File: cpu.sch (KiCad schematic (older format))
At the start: 12 parts, among them SW2 RESET_SW, U10 NE555, U2 MOS_8501, U9 74LS06

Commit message: Fix for KiCad 5.1.7
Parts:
- removed U10: NE555, Package_DIP:DIP-8_W7.62mm_Socket_LongPads, symbol Timer:NE555
- added U10: NE555P, Package_DIP:DIP-8_W7.62mm_LongPads, symbol Timer:NE555P
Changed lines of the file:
@@
 Sheet 2 11
 Title "LittleSixteen"
-Date "2020-01-03"
+Date "2020-12-20"
 Rev "1git"
 Comp "SukkoPera"
@@
 PHI0
 $Comp
-L Timer:NE555 U10
-U 1 1 5EC2982D
-P 7885 2420
-F 0 "U10" H 7625 2765 50  0000 C CNN
-F 1 "NE555" H 7660 2070 50  0000 C CNN
-F 2 "Package_DIP:DIP-8_W7.62mm_Socket_LongPads" H 7885 2420 50  0001 C CNN
-F 3 "http://www.ti.com/lit/ds/symlink/ne555.pdf" H 7885 2420 50  0001 C CNN
-	1    7885 2420
-	-1   0    0    -1
-$EndComp
-$Comp
 L 74xx:74LS06 U9
 U 1 1 5EC2AC8D
@@
 Text GLabel 6320 1435 2    50   Output ~ 0
 ~RESET
+$Comp
+L Timer:NE555P U10
+U 1 1 5FE24901
+P 7885 2420
+F 0 "U10" H 7610 2770 50  0000 C CNN
+F 1 "NE555P" H 7685 2065 50  0000 C CNN
+F 2 "Package_DIP:DIP-8_W7.62mm_LongPads" H 8535 2020 50  0001 C CNN
+F 3 "http://www.ti.com/lit/ds/symlink/ne555.pdf" H 8735 2020 50  0001 C CNN
+	1    7885 2420
+	-1   0    0    -1
+$EndComp
 Wire Bus Line
 	5035 4120 5035 4580

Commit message: Start working on PCB
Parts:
- C16, C17, C4: footprint (none) -> Capacitor_THT:CP_Radial_D6.3mm_P2.50mm
- R19, R20, R21: footprint (none) -> Resistor_THT:R_Axial_DIN0207_L6.3mm_D2.5mm_P5.08mm_Vertical
- RP1: footprint (none) -> Resistor_THT:R_Array_SIP6
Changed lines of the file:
@@
 F 0 "C4" H 911 7136 50  0000 R CNN
 F 1 "10u/25V" H 911 7045 50  0000 R CNN
-F 2 "" H 1025 7090 50  0001 C CNN
+F 2 "Capacitor_THT:CP_Radial_D6.3mm_P2.50mm" H 1025 7090 50  0001 C CNN
 F 3 "~" H 1025 7090 50  0001 C CNN
 	1    1025 7090
@@
 F 0 "R19" H 2355 2016 50  0000 R CNN
 F 1 "3.3k" H 2355 1925 50  0000 R CNN
-F 2 "" V 2355 1970 50  0001 C CNN
+F 2 "Resistor_THT:R_Axial_DIN0207_L6.3mm_D2.5mm_P5.08mm_Vertical" V 2355 1970 50  0001 C CNN
 F 3 "~" H 2425 1970 50  0001 C CNN
 	1    2425 1970
@@
 F 0 "C16" H 7200 2981 50  0000 L CNN
 F 1 "10u/25V" H 7200 2890 50  0000 L CNN
-F 2 "" H 7085 2935 50  0001 C CNN
+F 2 "Capacitor_THT:CP_Radial_D6.3mm_P2.50mm" H 7085 2935 50  0001 C CNN
 F 3 "~" H 7085 2935 50  0001 C CNN
 	1    7085 2935
@@
 F 0 "R20" H 7155 1971 50  0000 L CNN
 F 1 "47k" H 7155 1880 50  0000 L CNN
-F 2 "" V 7015 1925 50  0001 C CNN
+F 2 "Resistor_THT:R_Axial_DIN0207_L6.3mm_D2.5mm_P5.08mm_Vertical" V 7015 1925 50  0001 C CNN
 F 3 "~" H 7085 1925 50  0001 C CNN
 	1    7085 1925
@@
 F 0 "R21" H 9525 1971 50  0000 L CNN
 F 1 "100k" H 9525 1880 50  0000 L CNN
-F 2 "" V 9385 1925 50  0001 C CNN
+F 2 "Resistor_THT:R_Axial_DIN0207_L6.3mm_D2.5mm_P5.08mm_Vertical" V 9385 1925 50  0001 C CNN
 F 3 "~" H 9455 1925 50  0001 C CNN
 	1    9455 1925
@@
 F 0 "C17" H 8961 2731 50  0000 R CNN
 F 1 "1u/16V" H 8961 2640 50  0000 R CNN
-F 2 "" H 9075 2685 50  0001 C CNN
+F 2 "Capacitor_THT:CP_Radial_D6.3mm_P2.50mm" H 9075 2685 50  0001 C CNN
 F 3 "~" H 9075 2685 50  0001 C CNN
 	1    9075 2685
@@
 F 0 "RP1" H 4613 1966 50  0000 L CNN
 F 1 "1k" H 4613 1875 50  0000 L CNN
-F 2 "" V 4455 1920 50  0001 C CNN
+F 2 "Resistor_THT:R_Array_SIP6" V 4455 1920 50  0001 C CNN
 F 3 "~" H 4525 1920 50  0001 C CNN
 	1    4525 1920

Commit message: Add ceramics
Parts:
- C22: footprint (none) -> Capacitor_THT:C_Disc_D8.0mm_W2.5mm_P5.00mm
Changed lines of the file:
@@
 F 0 "C22" H 1635 7136 50  0000 L CNN
 F 1 "100n" H 1635 7045 50  0000 L CNN
-F 2 "" H 1558 6940 50  0001 C CNN
+F 2 "Capacitor_THT:C_Disc_D8.0mm_W2.5mm_P5.00mm" H 1558 6940 50  0001 C CNN
 F 3 "~" H 1520 7090 50  0001 C CNN
 	1    1520 7090

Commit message: Use 3d models from github.com/StormTrooper/Commodore-Plus4
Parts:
- SW2: footprint (none) -> CommodorePlus4:Switch-Pushbutton
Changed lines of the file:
@@
 F 0 "SW2" V 9409 2793 50  0000 L CNN
 F 1 "RESET_SW" V 9500 2793 50  0000 L CNN
-F 2 "" H 9455 2685 60  0001 C CNN
+F 2 "CommodorePlus4:Switch-Pushbutton" H 9455 2685 60  0001 C CNN
 F 3 "" H 9455 2685 60  0000 C CNN
 	1    9455 2685

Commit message: Working on PCB...
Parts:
- SW2: footprint CommodorePlus4:Switch-Pushbutton -> LittleSixteen:Switch-Pushbutton
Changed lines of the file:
@@
 F 0 "SW2" V 9409 2793 50  0000 L CNN
 F 1 "RESET_SW" V 9500 2793 50  0000 L CNN
-F 2 "CommodorePlus4:Switch-Pushbutton" H 9455 2685 60  0001 C CNN
+F 2 "LittleSixteen:Switch-Pushbutton" H 9455 2685 60  0001 C CNN
 F 3 "" H 9455 2685 60  0000 C CNN
 	1    9455 2685

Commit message: A whole looooooot of work
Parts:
- U10: footprint Package_DIP:DIP-8_W7.62mm_LongPads -> Package_DIP:DIP-8_W7.62mm_Socket_LongPads
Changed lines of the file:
@@
 F 0 "U10" H 7610 2770 50  0000 C CNN
 F 1 "NE555P" H 7685 2065 50  0000 C CNN
-F 2 "Package_DIP:DIP-8_W7.62mm_LongPads" H 8535 2020 50  0001 C CNN
+F 2 "Package_DIP:DIP-8_W7.62mm_Socket_LongPads" H 8535 2020 50  0001 C CNN
 F 3 "http://www.ti.com/lit/ds/symlink/ne555.pdf" H 8735 2020 50  0001 C CNN
 	1    7885 2420

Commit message: Add extra decoupling caps There are actually (unnamed) footprints for these on an actual board, I guess they were skipped for cost saving reasons, sigh...
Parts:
- added C29: 100n, Capacitor_THT:C_Disc_D8.0mm_W2.5mm_P5.00mm, symbol Device:C
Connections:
- net GND: now also C29.2
- net VCC: now also C29.1
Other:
- note added: "Additional\ndecoupling cap\nfor U10"
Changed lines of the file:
@@
 Sheet 2 11
 Title "LittleSixteen"
-Date "2020-12-20"
+Date "2021-07-20"
 Rev "1git"
 Comp "SukkoPera"
@@
 	-1   0    0    -1
 $EndComp
+Wire Wire Line
+	10455 2595 10455 2670
+Wire Wire Line
+	10455 2220 10455 2295
+$Comp
+L power:GND #PWR?
+U 1 1 611CBEE7
+P 10455 2670
+AR Path="/5E4A465A/611CBEE7" Ref="#PWR?"  Part="1"
+AR Path="/5EE7AAEB/611CBEE7" Ref="#PWR?"  Part="1"
+AR Path="/5E4A81E1/611CBEE7" Ref="#PWR0133"  Part="1"
+F 0 "#PWR0133" H 10455 2420 50  0001 C CNN
+F 1 "GND" H 10460 2497 50  0000 C CNN
+F 2 "" H 10455 2670 50  0001 C CNN
+F 3 "" H 10455 2670 50  0001 C CNN
+	1    10455 2670
+	1    0    0    -1
+$EndComp
+$Comp
+L power:VCC #PWR?
+U 1 1 611CBEED
+P 10455 2220
+AR Path="/5E4A465A/611CBEED" Ref="#PWR?"  Part="1"
+AR Path="/5EE7AAEB/611CBEED" Ref="#PWR?"  Part="1"
+AR Path="/5E4A81E1/611CBEED" Ref="#PWR0134"  Part="1"
+F 0 "#PWR0134" H 10455 2070 50  0001 C CNN
+F 1 "VCC" H 10472 2393 50  0000 C CNN
+F 2 "" H 10455 2220 50  0001 C CNN
+F 3 "" H 10455 2220 50  0001 C CNN
+	1    10455 2220
+	1    0    0    -1
+$EndComp
+$Comp
+L Device:C C?
+U 1 1 611CBEF3
+P 10455 2445
+AR Path="/5E4A465A/611CBEF3" Ref="C?"  Part="1"
+AR Path="/5EE7AAEB/611CBEF3" Ref="C?"  Part="1"
+AR Path="/5E4A81E1/611CBEF3" Ref="C29"  Part="1"
+F 0 "C29" H 10570 2491 50  0000 L CNN
+F 1 "100n" H 10570 2400 50  0000 L CNN
+F 2 "Capacitor_THT:C_Disc_D8.0mm_W2.5mm_P5.00mm" H 10493 2295 50  0001 C CNN
+F 3 "~" H 10455 2445 50  0001 C CNN
+	1    10455 2445
+	1    0    0    -1
+$EndComp
+Text Notes 10225 3190 0    50   ~ 0
+Additional\ndecoupling cap\nfor U10
 Wire Bus Line
 	5035 4120 5035 4580

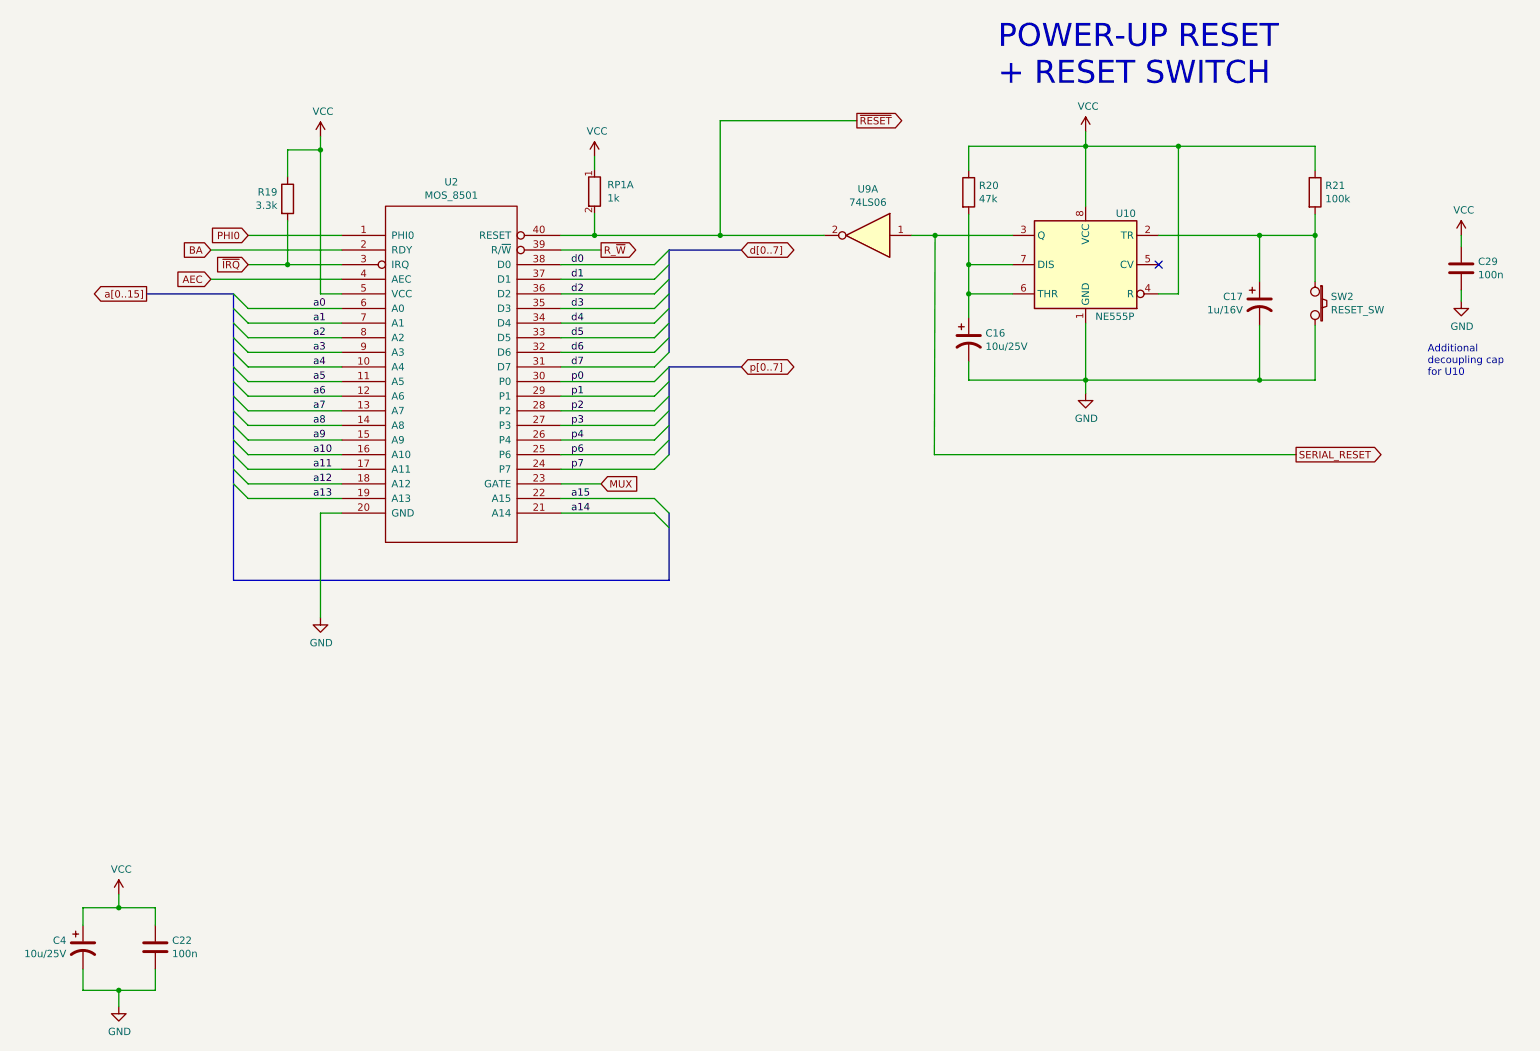
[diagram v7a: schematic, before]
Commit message: Move POR to misc, review some notes
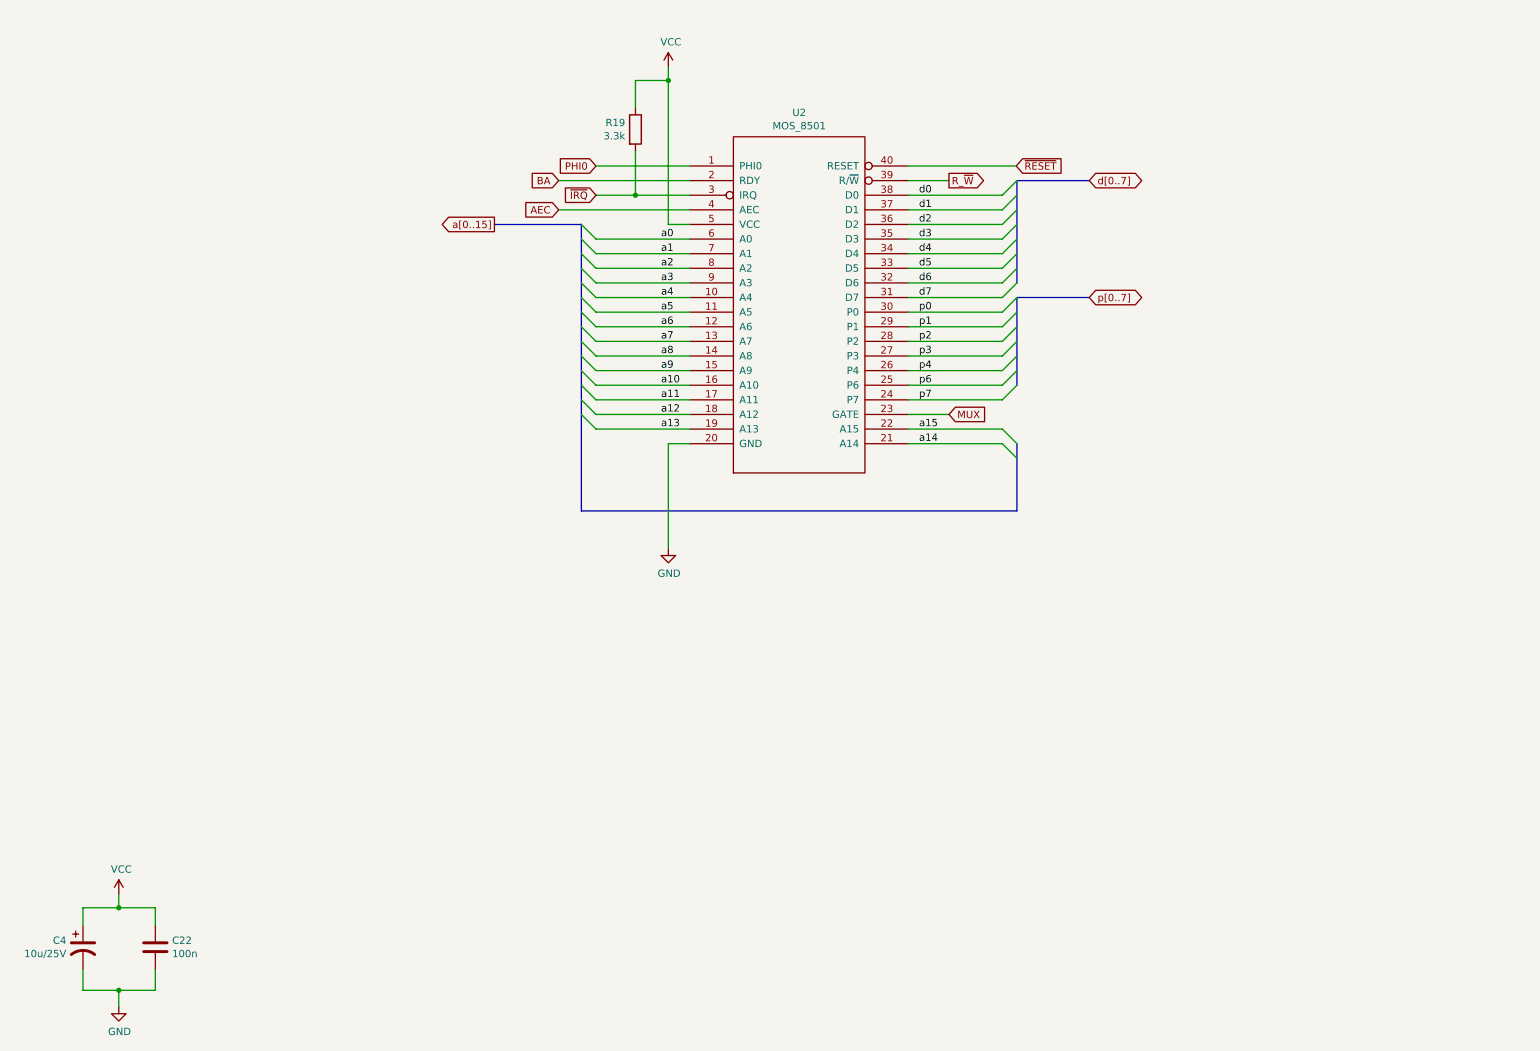
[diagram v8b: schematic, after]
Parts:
- removed C16: 10u/25V, Capacitor_THT:CP_Radial_D6.3mm_P2.50mm, symbol Device:CP1
- removed C17: 1u/16V, Capacitor_THT:CP_Radial_D6.3mm_P2.50mm, symbol Device:CP1
- removed C29: 100n, Capacitor_THT:C_Disc_D8.0mm_W2.5mm_P5.00mm, symbol Device:C
- removed R20: 47k, Resistor_THT:R_Axial_DIN0207_L6.3mm_D2.5mm_P5.08mm_Vertical, symbol Device:R
- removed R21: 100k, Resistor_THT:R_Axial_DIN0207_L6.3mm_D2.5mm_P5.08mm_Vertical, symbol Device:R
- removed RP1: 1k, Resistor_THT:R_Array_SIP6, symbol r_pack05:R_Pack_5_Split
- removed SW2: RESET_SW, LittleSixteen:Switch-Pushbutton, symbol w_device:SW_PUSH
- removed U10: NE555P, Package_DIP:DIP-8_W7.62mm_Socket_LongPads, symbol Timer:NE555P
- removed U9: 74LS06, Package_DIP:DIP-14_W7.62mm_Socket_LongPads, symbol 74xx:74LS06
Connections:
- no-connect marks 1 -> 0
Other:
- note removed: "Additional\ndecoupling cap\nfor U10"
- note removed: "POWER-UP RESET\n+ RESET SWITCH"
- moved on the sheet: R19, U2
